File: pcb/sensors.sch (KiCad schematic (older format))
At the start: 6 parts, among them J2 Conn_01x04_Male, Q2 BSS138DW-7-F, U4 BME280, U6 SGP30, U7 TSL2591

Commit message: finish laying out most of the pcb parts
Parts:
- removed Q2: BSS138DW-7-F, digikey-footprints:SOT-363, symbol pcb-rescue:BSS138DW-7-F-dk_Transistors-FETs-MOSFETs-Arrays
- removed RN1: 10k, Resistor_SMD:R_Array_Convex_4x0603, symbol Device:R_Pack04_Split
- removed U4: BME280, digikey-footprints:Pressure_Sensor_LGA-8_2.5x2.5mm_BME280, symbol pcb-rescue:BME280-dk_Humidity-Moisture-Sensors
- removed U6: SGP30, Kevin_Lutzer:SGP30, symbol pcb-rescue:SGP30-Kevin_Lutzer
- removed U7: TSL2591, Kevin_Lutzer:TSL2591, symbol pcb-rescue:TSL2591-Kevin_Lutzer
- added C11, C12, C3: 100n, Capacitor_SMD:C_0603_1608Metric, symbol Device:C
- added Q2: BSS138DW-7-F, digikey-footprints:SOT-363, symbol dk_Transistors-FETs-MOSFETs-Arrays:BSS138DW-7-F
- added R10, R11, R12, R13: 10k, Resistor_SMD:R_0603_1608Metric, symbol Device:R_US
- added U4: BME280, digikey-footprints:Pressure_Sensor_LGA-8_2.5x2.5mm_BME280, symbol dk_Humidity-Moisture-Sensors:BME280
- added U6: SGP30, SGP30 (1):SGP30, symbol Kevin_Lutzer:SGP30
- added U7: TSL2591, Package_DFN_QFN:DFN-6_1.3x1.2mm_P0.4mm, symbol Kevin_Lutzer:TSL2591
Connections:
- wire segments 53 -> 59
- no-connect marks 2 -> 3

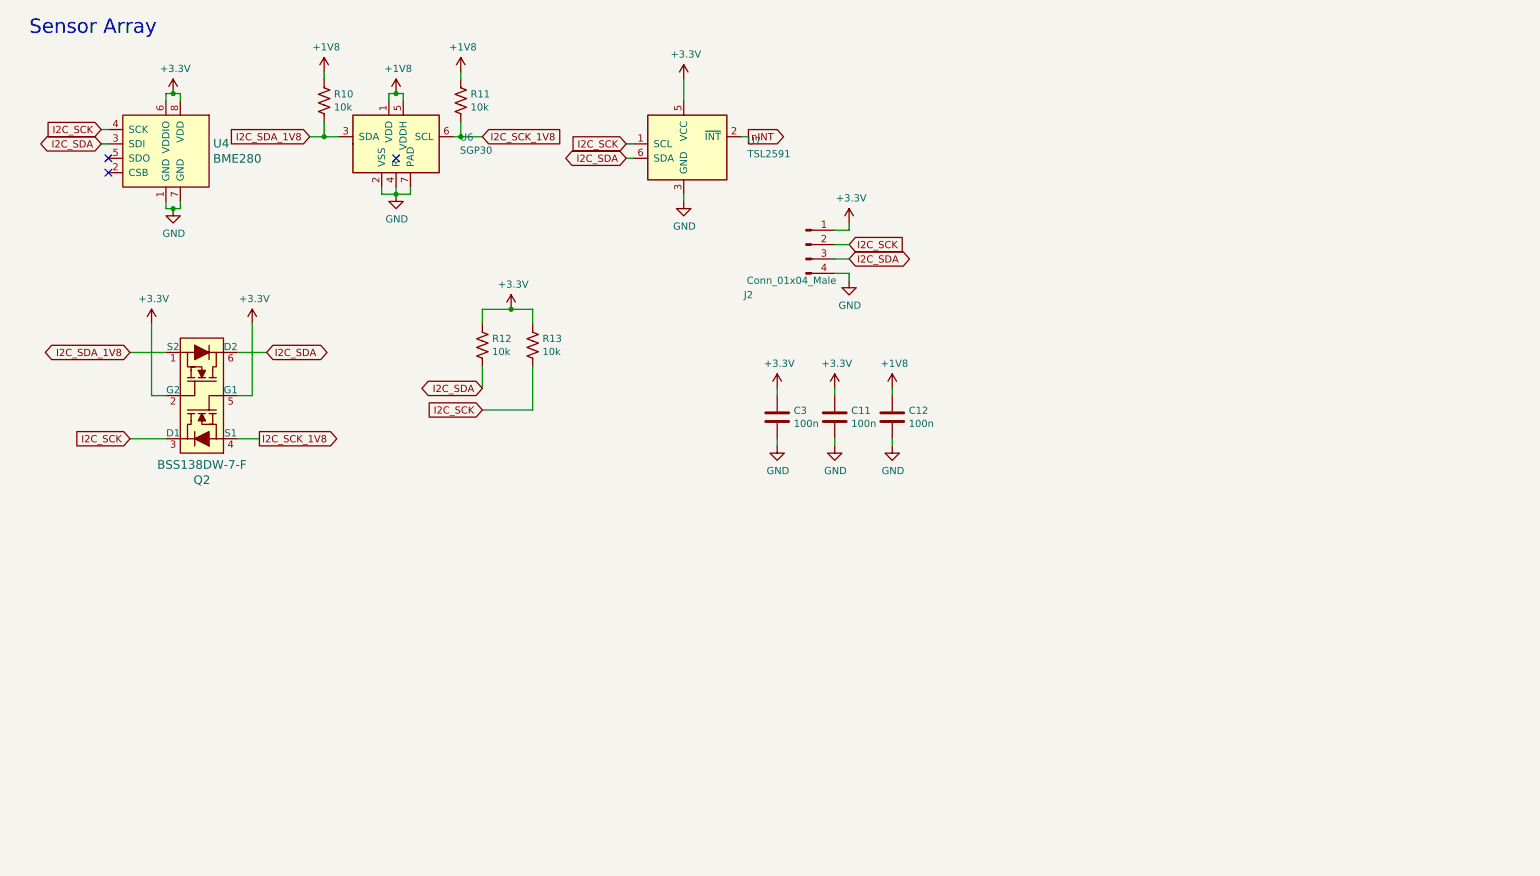
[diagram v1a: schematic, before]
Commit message: finish the routing of the pcb all that is left is to clean up the silkscreen
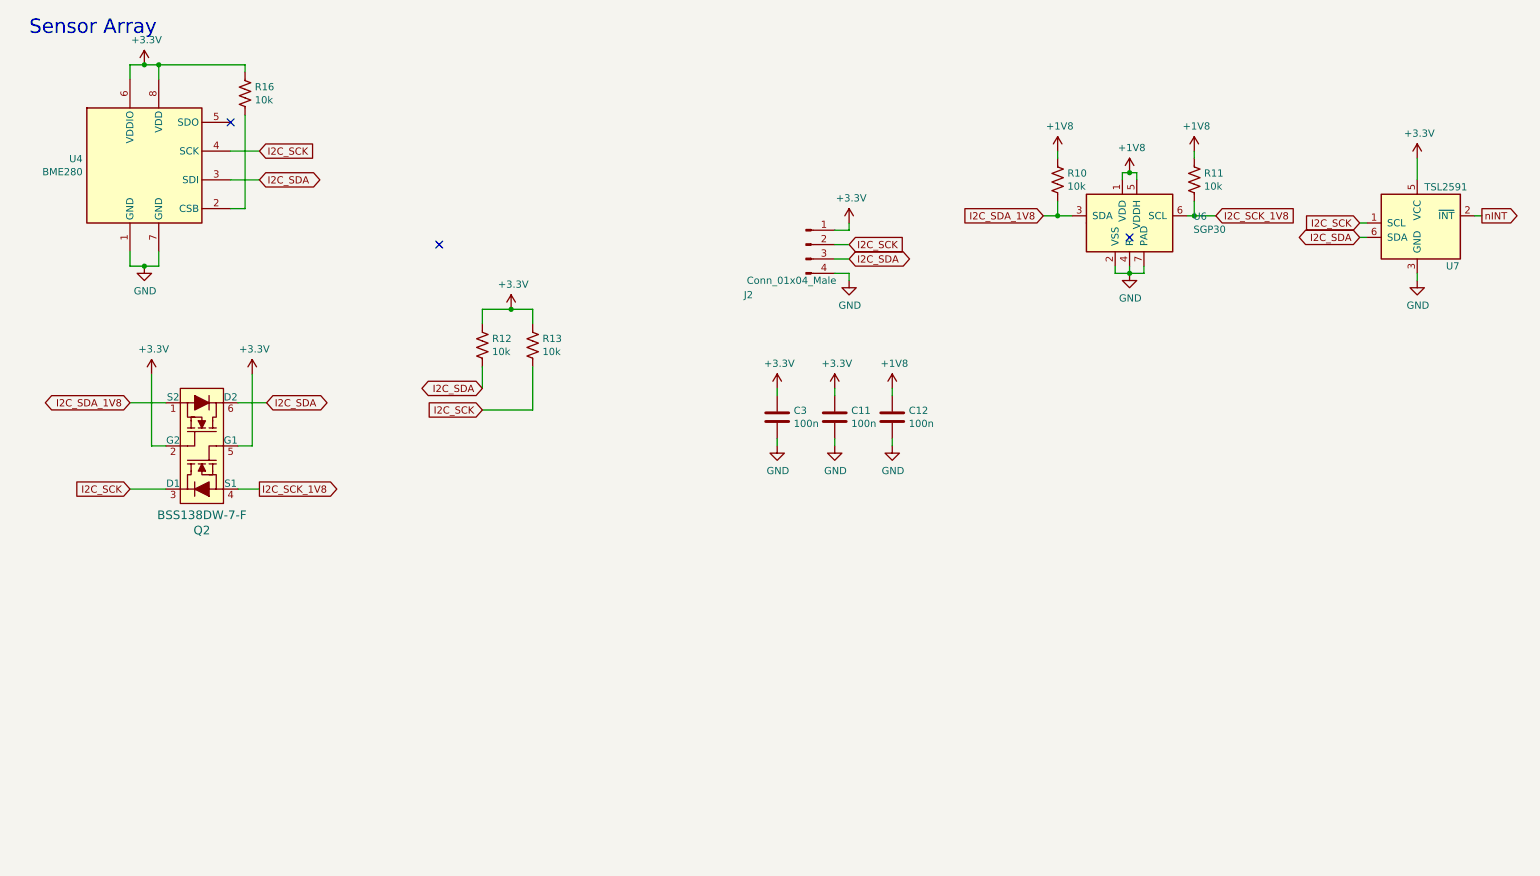
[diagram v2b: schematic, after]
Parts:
- removed U4: BME280, digikey-footprints:Pressure_Sensor_LGA-8_2.5x2.5mm_BME280, symbol dk_Humidity-Moisture-Sensors:BME280
- added R16: 10k, Resistor_SMD:R_0603_1608Metric, symbol Device:R_US
- added U4: BME280, Package_LGA:Bosch_LGA-8_2.5x2.5mm_P0.65mm_ClockwisePinNumbering, symbol Sensor:BME280
- U7: footprint Package_DFN_QFN:DFN-6_1.3x1.2mm_P0.4mm -> Kevin-Lutzer-Kicad-Lbr:TSL2591
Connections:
- net +3V3: now also R16.1, U4.6 (VDDIO), U4.8 (VDD)
- net GND: now also U4.1 (GND), U4.7 (GND)
- net I2C_SCK: now also U4.4 (SCK)
- net I2C_SDA: now also U4.3 (SDI)
- new net: R16.2, U4.2 (CSB)
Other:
- moved on the sheet: Q2, R10, R11, U7

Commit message: add gerbers for room monitor v1
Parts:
- J2: value Conn_01x04_Male -> I2C_BUS
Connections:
- no-connect marks 3 -> 1
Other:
- note added: "Bypass Caps"
- note added: "I2C Buss Connector"
- note added: "Lvl shifter from 1.8V to 3.3V"
- note added: "Pullups for the I2C Bus"
- note added: "Sensor Address\nBME280 - 0x77\nTSL2591 - 0x29\nSGP30 - 0x58"
- moved on the sheet: C11, C12, C3, J2, Q2, R10, R11, R12, R13, R16, U4, U6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

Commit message: Update the gerbers for the rem v1 and reroute the UART lines
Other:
- note removed: "Bypass Caps"
- note removed: "I2C Buss Connector"
- note removed: "Pullups for the I2C Bus"
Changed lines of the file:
@@
 Text Notes 1750 2550 0    50   ~ 0
 Sensor Address\nBME280 - 0x77\nTSL2591 - 0x29\nSGP30 - 0x58
-Text Notes 4250 3250 0    50   ~ 0
-Bypass Caps
 Text Notes 1150 3250 0    50   ~ 0
 Lvl shifter from 1.8V to 3.3V
-Text Notes 3200 3250 0    50   ~ 0
-I2C Buss Connector
-Text Notes 5950 3250 0    50   ~ 0
-Pullups for the I2C Bus
 $Comp
 L Kevin_Lutzer:SGP30 U6

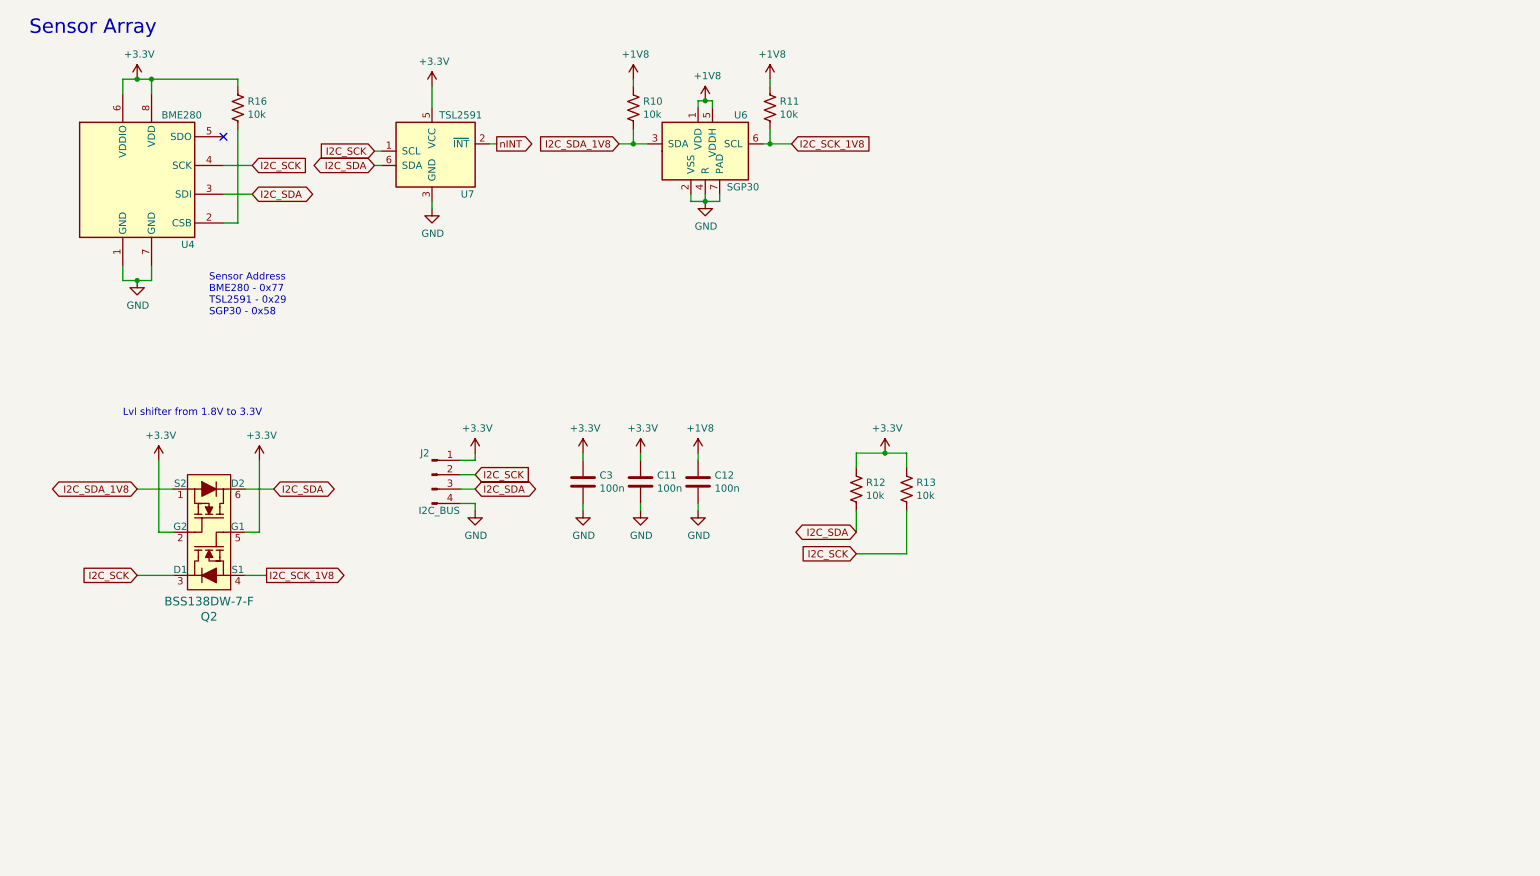
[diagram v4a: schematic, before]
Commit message: cleanup sensors sheet
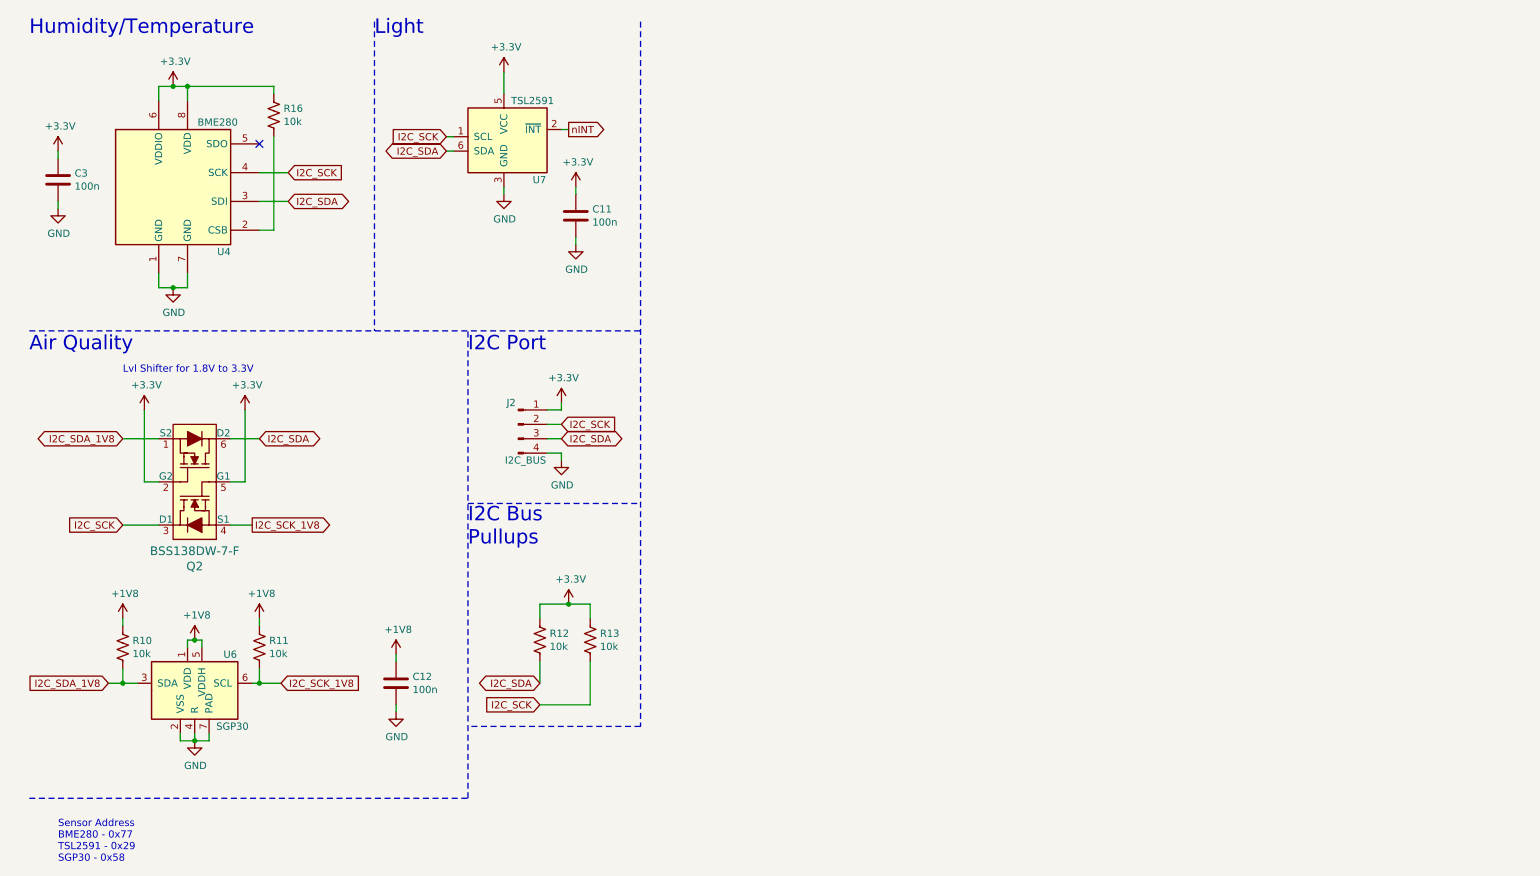
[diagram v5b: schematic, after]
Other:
- note added: "Air Quality"
- note added: "Humidity/Temperature"
- note added: "I2C Bus\nPullups"
- note added: "I2C Port"
- note added: "Light"
- note added: "Lvl Shifter for 1.8V to 3.3V"
- note removed: "Lvl shifter from 1.8V to 3.3V"
- note removed: "Sensor Array"
- moved on the sheet: C11, C12, C3, J2, Q2, R10, R11, R12, R13, R16, U4, U6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

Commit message: add more comments to the pcb, cleanup board files
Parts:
- U6: footprint SGP30 (1):SGP30 -> Kevin-Lutzer-Kicad-Lbr:SGP30
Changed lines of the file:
@@
 F 0 "U6" H 1850 5400 50  0000 L CNN
 F 1 "SGP30" H 1800 4900 50  0000 L CNN
-F 2 "SGP30 (1):SGP30" H 1600 5850 50  0001 C CNN
+F 2 "Kevin-Lutzer-Kicad-Lbr:SGP30" H 1600 5850 50  0001 C CNN
 F 3 "" H 1650 5100 50  0001 C CNN
 	1    1650 5150

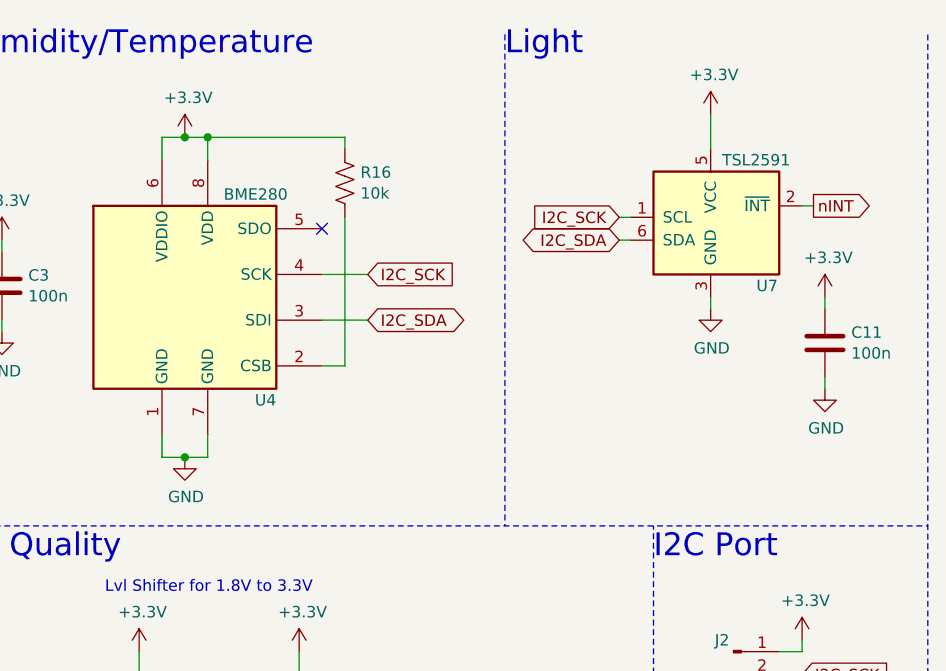
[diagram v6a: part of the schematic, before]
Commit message: update the footprint for the tsl2591
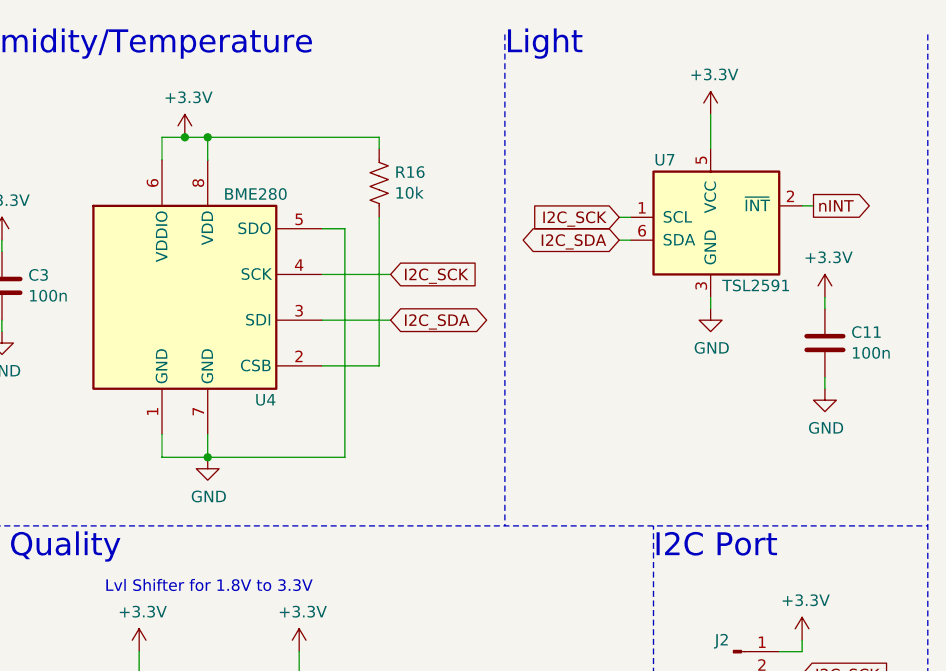
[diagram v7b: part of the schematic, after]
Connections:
- net GND: now also U4.5 (SDO)
- no-connect marks 1 -> 0
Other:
- moved on the sheet: R16
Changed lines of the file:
@@
 Comment4 ""
 $EndDescr
-Text GLabel 2300 1550 2    50   Input ~ 0
+Text GLabel 2400 1550 2    50   Input ~ 0
 I2C_SCK
-Text GLabel 2300 1750 2    50   BiDi ~ 0
+Text GLabel 2400 1750 2    50   BiDi ~ 0
 I2C_SDA
 $Comp
@@
 Text GLabel 3400 1400 0    50   BiDi ~ 0
 I2C_SDA
-$Comp
-L Kevin_Lutzer:TSL2591 U7
-U 1 1 5F2329EE
-P 3850 1350
-F 0 "U7" H 4000 1100 50  0000 L CNN
-F 1 "TSL2591" H 3850 1650 50  0000 L CNN
-F 2 "Kevin-Lutzer-Kicad-Lbr:TSL2591" H 3300 1100 50  0001 C CNN
-F 3 "https://cdn-shop.adafruit.com/datasheets/TSL25911_Datasheet_EN_v1.pdf" H 3800 1400 50  0001 C CNN
-	1    3850 1350
-	1    0    0    -1
-$EndComp
 $Comp
 L dk_Transistors-FETs-MOSFETs-Arrays:BSS138DW-7-F Q2
@@
 	1600 950  1600 1050
 Wire Wire Line
-	2300 1550 2100 1550
+	2400 1550 2100 1550
 $Comp
 L power:GND #PWR?
 U 1 1 5F5F0DAC
-P 1500 2350
+P 1600 2350
 AR Path="/5F5F0DAC" Ref="#PWR?"  Part="1"
 AR Path="/5F9A85F1/5F5F0DAC" Ref="#PWR0109"  Part="1"
-F 0 "#PWR0109" H 1500 2100 50  0001 C CNN
-F 1 "GND" H 1505 2177 50  0000 C CNN
-F 2 "" H 1500 2350 50  0001 C CNN
-F 3 "" H 1500 2350 50  0001 C CNN
-	1    1500 2350
+F 0 "#PWR0109" H 1600 2100 50  0001 C CNN
+F 1 "GND" H 1605 2177 50  0000 C CNN
+F 2 "" H 1600 2350 50  0001 C CNN
+F 3 "" H 1600 2350 50  0001 C CNN
+	1    1600 2350
 	1    0    0    -1
 $EndComp
@@
 	1400 2250 1400 2350
 Wire Wire Line
-	1400 2350 1500 2350
-Wire Wire Line
-	1500 2350 1600 2350
+	1400 2350 1600 2350
 Wire Wire Line
 	1600 2350 1600 2250
-Connection ~ 1500 2350
+Connection ~ 1600 2350
 $Comp
 L power:+3.3V #PWR?
@@
 Wire Wire Line
 	1500 950  1600 950
-NoConn ~ 2100 1350
 $Comp
 L Device:R_US R16
 U 1 1 5F61590D
-P 2200 1150
-F 0 "R16" H 2268 1196 50  0000 L CNN
-F 1 "10k" H 2268 1105 50  0000 L CNN
-F 2 "Resistor_SMD:R_0603_1608Metric" V 2240 1140 50  0001 C CNN
-F 3 "~" H 2200 1150 50  0001 C CNN
-	1    2200 1150
-	1    0    0    -1
-$EndComp
-Wire Wire Line
-	2200 1000 2200 950
-Wire Wire Line
-	2100 1950 2200 1950
-Wire Wire Line
-	2200 1300 2200 1950
-Wire Wire Line
-	1600 950  2200 950
+P 2350 1150
+F 0 "R16" H 2418 1196 50  0000 L CNN
+F 1 "10k" H 2418 1105 50  0000 L CNN
+F 2 "Resistor_SMD:R_0603_1608Metric" V 2390 1140 50  0001 C CNN
+F 3 "~" H 2350 1150 50  0001 C CNN
+	1    2350 1150
+	1    0    0    -1
+$EndComp
+Wire Wire Line
+	2350 1000 2350 950
+Wire Wire Line
+	2100 1950 2350 1950
+Wire Wire Line
+	2350 1300 2350 1950
+Wire Wire Line
+	1600 950  2350 950
 Connection ~ 1600 950
 Wire Wire Line
-	2100 1750 2300 1750
+	2100 1750 2400 1750
 Text Notes 700  6350 0    50   ~ 0
 Sensor Address\nBME280 - 0x77\nTSL2591 - 0x29\nSGP30 - 0x58
@@
 Text Notes 3550 4150 0    100  ~ 0
 I2C Bus\nPullups
+Wire Wire Line
+	1600 2350 2200 2350
+Wire Wire Line
+	2200 2350 2200 1350
+Wire Wire Line
+	2200 1350 2100 1350
+$Comp
+L Kevin_Lutzer:TSL2591 U7
+U 1 1 5F50BFF8
+P 3850 1350
+F 0 "U7" H 3600 1650 50  0000 C CNN
+F 1 "TSL2591" H 4000 1100 50  0000 C CNN
+F 2 "Kevin-Lutzer-Kicad-Lbr:TSL2591" H 3300 1100 50  0001 C CNN
+F 3 "https://cdn-shop.adafruit.com/datasheets/TSL25911_Datasheet_EN_v1.pdf" H 3800 1400 50  0001 C CNN
+	1    3850 1350
+	1    0    0    -1
+$EndComp
 $EndSCHEMATC
